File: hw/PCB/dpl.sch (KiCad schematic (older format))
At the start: 1 part

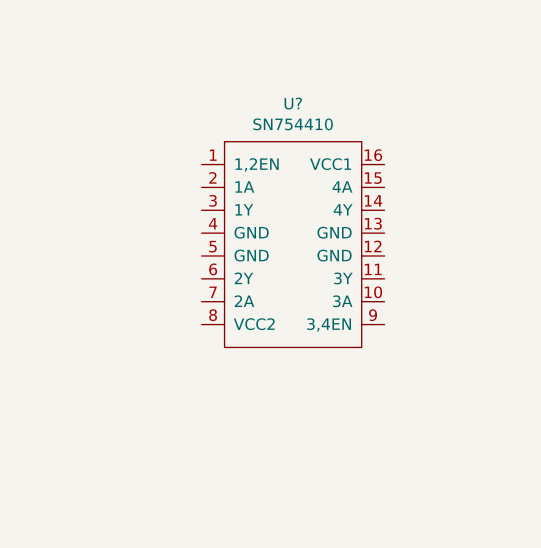
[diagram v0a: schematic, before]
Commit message: Added pin labels for the femto-satellite deploy system.
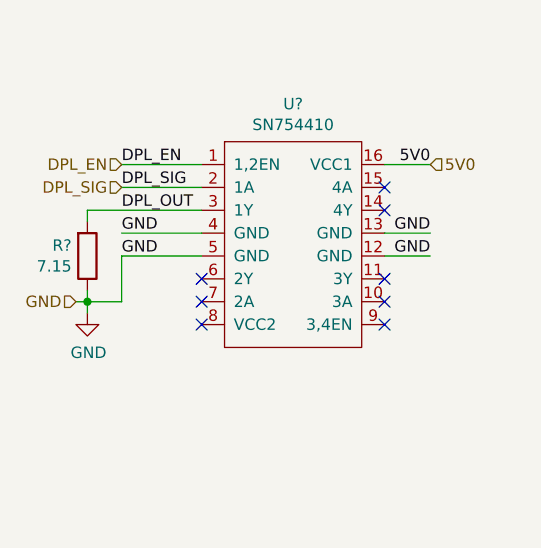
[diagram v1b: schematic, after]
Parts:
- added R?: 7.15, symbol Device:R
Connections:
- net DPL_EN: now reaches U?.1 (1,2EN)
- net GND: now reaches U?.12 (GND)
- net GND: now also U?.13 (GND), U?.4 (GND), U?.5 (GND), R?.1
- net 5V0: now reaches U?.16 (VCC1)
- net DPL_SIG: now reaches U?.2 (1A)
- net DPL_OUT: now reaches U?.3 (1Y)
- net DPL_OUT: now also R?.2
- no-connect marks 0 -> 8
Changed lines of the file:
@@
 	1    0    0    -1
 $EndComp
+$Comp
+L Device:R R?
+U 1 1 5BEA225C
+P 4750 3500
+F 0 "R?" H 4681 3454 50  0000 R CNN
+F 1 "7.15" H 4681 3545 50  0000 R CNN
+F 2 "" V 4680 3500 50  0001 C CNN
+F 3 "~" H 4750 3500 50  0001 C CNN
+	1    4750 3500
+	1    0    0    1
+$EndComp
+Wire Wire Line
+	6050 3100 6250 3100
+Text Label 6250 3100 2    50   ~ 0
+5V0
+Text Label 4900 3200 0    50   ~ 0
+DPL_SIG
+Text Label 4900 3100 0    50   ~ 0
+DPL_EN
+Text Label 4900 3300 0    50   ~ 0
+DPL_OUT
+Wire Wire Line
+	5250 3100 4900 3100
+Wire Wire Line
+	4900 3200 5250 3200
+Wire Wire Line
+	5250 3400 4900 3400
+Wire Wire Line
+	4900 3500 5250 3500
+Wire Wire Line
+	6050 3400 6250 3400
+Wire Wire Line
+	6250 3500 6050 3500
+Text Label 4900 3400 0    50   ~ 0
+GND
+Text Label 4900 3500 0    50   ~ 0
+GND
+Text Label 6250 3400 2    50   ~ 0
+GND
+Text Label 6250 3500 2    50   ~ 0
+GND
+Wire Wire Line
+	4750 3300 4750 3350
+Wire Wire Line
+	4750 3300 5250 3300
+Wire Wire Line
+	4750 3650 4750 3700
+Wire Wire Line
+	4750 3700 4900 3700
+Wire Wire Line
+	4900 3700 4900 3500
+Wire Wire Line
+	4750 3700 4750 3750
+Connection ~ 4750 3700
+$Comp
+L power:GND #PWR?
+U 1 1 5BEA3F1A
+P 4750 3750
+F 0 "#PWR?" H 4750 3500 50  0001 C CNN
+F 1 "GND" H 4755 3577 50  0000 C CNN
+F 2 "" H 4750 3750 50  0001 C CNN
+F 3 "" H 4750 3750 50  0001 C CNN
+	1    4750 3750
+	1    0    0    -1
+$EndComp
+Text HLabel 4900 3100 0    50   Input ~ 0
+DPL_EN
+Text HLabel 4900 3200 0    50   Input ~ 0
+DPL_SIG
+Text HLabel 4700 3700 0    50   Input ~ 0
+GND
+Wire Wire Line
+	4750 3700 4700 3700
+NoConn ~ 6050 3200
+NoConn ~ 6050 3300
+NoConn ~ 6050 3600
+NoConn ~ 6050 3700
+NoConn ~ 6050 3800
+NoConn ~ 5250 3600
+NoConn ~ 5250 3700
+NoConn ~ 5250 3800
+Text HLabel 6250 3100 2    50   Input ~ 0
+5V0
 $EndSCHEMATC

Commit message: Updated the connections and the footprints asignation.
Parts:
- U3: renamed from U?; footprint (none) -> Package_DIP:DIP-16_W7.62mm_Socket_LongPads
- gave numbers to parts that had none: 1
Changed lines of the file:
@@
 $EndDescr
 $Comp
-L H-Bridge:SN754410 U?
+L H-Bridge:SN754410 U3
 U 1 1 5BEA29D2
 P 5650 3450
-F 0 "U?" H 5650 4065 50  0000 C CNN
+F 0 "U3" H 5650 4065 50  0000 C CNN
 F 1 "SN754410" H 5650 3974 50  0000 C CNN
-F 2 "" H 5500 3550 50  0001 C CNN
+F 2 "Package_DIP:DIP-16_W7.62mm_Socket_LongPads" H 5500 3550 50  0001 C CNN
 F 3 "" H 5500 3550 50  0001 C CNN
 	1    5650 3450
@@
 $EndComp
 $Comp
-L Device:R R?
+L Device:R R3
 U 1 1 5BEA225C
 P 4750 3500
-F 0 "R?" H 4681 3454 50  0000 R CNN
+F 0 "R3" H 4681 3454 50  0000 R CNN
 F 1 "7.15" H 4681 3545 50  0000 R CNN
 F 2 "" V 4680 3500 50  0001 C CNN
@@
 Connection ~ 4750 3700
 $Comp
-L power:GND #PWR?
+L power:GND #PWR0112
 U 1 1 5BEA3F1A
 P 4750 3750
-F 0 "#PWR?" H 4750 3500 50  0001 C CNN
+F 0 "#PWR0112" H 4750 3500 50  0001 C CNN
 F 1 "GND" H 4755 3577 50  0000 C CNN
 F 2 "" H 4750 3750 50  0001 C CNN

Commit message: Added the deployment system to the board's footprint.
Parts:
- R3: footprint (none) -> Resistor_FOD:RCL12257R15FKEG
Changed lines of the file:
@@
 F 0 "R3" H 4681 3454 50  0000 R CNN
 F 1 "7.15" H 4681 3545 50  0000 R CNN
-F 2 "" V 4680 3500 50  0001 C CNN
+F 2 "Resistor_FOD:RCL12257R15FKEG" V 4680 3500 50  0001 C CNN
 F 3 "~" H 4750 3500 50  0001 C CNN
 	1    4750 3500

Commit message: Added new connections and 3D models. Most components are now placed in the PCB.
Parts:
- U3: footprint Package_DIP:DIP-16_W7.62mm_Socket_LongPads -> Package_DIP:DIP-16_W7.62mm_LongPads
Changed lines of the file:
@@
 F 0 "U3" H 5650 4065 50  0000 C CNN
 F 1 "SN754410" H 5650 3974 50  0000 C CNN
-F 2 "Package_DIP:DIP-16_W7.62mm_Socket_LongPads" H 5500 3550 50  0001 C CNN
+F 2 "Package_DIP:DIP-16_W7.62mm_LongPads" H 5500 3550 50  0001 C CNN
 F 3 "" H 5500 3550 50  0001 C CNN
 	1    5650 3450

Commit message: Added switch to detect the deplyment status. Routed all connections.
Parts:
- added R4: 1K, Resistor_SMD:R_0603_1608Metric_Pad1.05x0.95mm_HandSolder, symbol Device:R
- added U5: AV4524_2PIN, Interrupt:AV4524_2PIN, symbol Interrupter:AV4524_2PIN
- U3: footprint Package_DIP:DIP-16_W7.62mm_LongPads -> Package_DIP:DIP-16_W7.62mm
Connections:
- net GND: now also U5.1 (COM)
- net 5V0 renamed VCC
- net VCC: now also R4.2
- new net DPL_STA: R4.1, U5.2 (NO)
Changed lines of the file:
@@
 F 0 "U3" H 5650 4065 50  0000 C CNN
 F 1 "SN754410" H 5650 3974 50  0000 C CNN
-F 2 "Package_DIP:DIP-16_W7.62mm_LongPads" H 5500 3550 50  0001 C CNN
+F 2 "Package_DIP:DIP-16_W7.62mm" H 5500 3550 50  0001 C CNN
 F 3 "" H 5500 3550 50  0001 C CNN
 	1    5650 3450
@@
 	6050 3100 6250 3100
 Text Label 6250 3100 2    50   ~ 0
-5V0
+VCC
 Text Label 4900 3200 0    50   ~ 0
 DPL_SIG
@@
 NoConn ~ 5250 3800
 Text HLabel 6250 3100 2    50   Input ~ 0
-5V0
+VCC
+$Comp
+L Device:R R4
+U 1 1 5BF60B18
+P 5150 4300
+F 0 "R4" H 5081 4254 50  0000 R CNN
+F 1 "1K" H 5081 4345 50  0000 R CNN
+F 2 "Resistor_SMD:R_0603_1608Metric_Pad1.05x0.95mm_HandSolder" V 5080 4300 50  0001 C CNN
+F 3 "~" H 5150 4300 50  0001 C CNN
+	1    5150 4300
+	1    0    0    1
+$EndComp
+Text Label 5250 4500 0    50   ~ 0
+DPL_STA
+Wire Wire Line
+	5250 4400 5550 4400
+Text Label 5250 4400 0    50   ~ 0
+GND
+Text Label 5000 4150 0    50   ~ 0
+VCC
+Wire Wire Line
+	5150 4150 5000 4150
+Wire Wire Line
+	5150 4500 5150 4450
+Wire Wire Line
+	5150 4500 5550 4500
+Wire Wire Line
+	5150 4500 5100 4500
+Connection ~ 5150 4500
+Text HLabel 5100 4500 0    50   Input ~ 0
+DPL_STA
+$Comp
+L Interrupter:AV4524_2PIN U5
+U 1 1 5BF65EF1
+P 5750 4500
+F 0 "U5" H 6028 4546 50  0000 L CNN
+F 1 "AV4524_2PIN" H 6028 4455 50  0000 L CNN
+F 2 "Interrupt:AV4524_2PIN" H 5700 4500 50  0001 C CNN
+F 3 "" H 5700 4500 50  0001 C CNN
+	1    5750 4500
+	1    0    0    -1
+$EndComp
 $EndSCHEMATC

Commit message: Finished preliminary design phase for the version 2.0.
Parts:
- removed R3: 7.15, Resistor_FOD:RCL12257R15FKEG, symbol Device:R
- removed R4: 1K, Resistor_SMD:R_0603_1608Metric_Pad1.05x0.95mm_HandSolder, symbol Device:R
- removed U3: SN754410, Package_DIP:DIP-16_W7.62mm, symbol H-Bridge:SN754410
- removed U5: AV4524_2PIN, Interrupt:AV4524_2PIN, symbol Interrupter:AV4524_2PIN
- added D2: LED, Diode_SMD:D_0805_2012Metric_Pad1.15x1.40mm_HandSolder, symbol Device:LED
- added J3: Nichrome, TerminalBlock:TerminalBlock_Altech_AK300-2_P5.00mm, symbol Connector:Screw_Terminal_01x02
- added Q1: PMV16XNR, Package_TO_SOT_SMD:SOT-23, symbol Transistor_FET:2N7002
- added R5: 330, Resistor_SMD:R_0603_1608Metric_Pad1.05x0.95mm_HandSolder, symbol Device:R
- added U4: AV4524, Interrupt:AV4524, symbol Interrupter:AV4524
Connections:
- net DPL_EN: now also D2.2 (A)
- net DPL_STA: now also U4.1 (COM)
- net GND: now also Q1.2 (S), R5.2, U4.3 (NC)
- new net: J3.2 (Pin_2), Q1.3 (D)
- new net: D2.1 (K), Q1.1 (G), R5.1
- new net 3V3: U4.2 (NO)
- new net VIN: J3.1 (Pin_1)
- no-connect marks 8 -> 0
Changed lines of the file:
@@
 EESchema Schematic File Version 5
-LIBS:FOD-cache
 EELAYER 29 0
 EELAYER END
 $Descr A4 11693 8268
 encoding utf-8
-Sheet 5 5
+Sheet 5 6
 Title ""
 Date ""
@@
 $EndDescr
 $Comp
-L H-Bridge:SN754410 U3
-U 1 1 5BEA29D2
-P 5650 3450
-F 0 "U3" H 5650 4065 50  0000 C CNN
-F 1 "SN754410" H 5650 3974 50  0000 C CNN
-F 2 "Package_DIP:DIP-16_W7.62mm" H 5500 3550 50  0001 C CNN
-F 3 "" H 5500 3550 50  0001 C CNN
-	1    5650 3450
+L power:GND #PWR0112
+U 1 1 5BEA3F1A
+P 5750 3150
+F 0 "#PWR0112" H 5750 2900 50  0001 C CNN
+F 1 "GND" H 5755 2977 50  0000 C CNN
+F 2 "" H 5750 3150 50  0001 C CNN
+F 3 "" H 5750 3150 50  0001 C CNN
+	1    5750 3150
+	1    0    0    -1
+$EndComp
+Text HLabel 4950 2900 0    50   Input ~ 0
+DPL_EN
+Text HLabel 4950 3950 0    50   Input ~ 0
+GND
+Text HLabel 5750 2550 0    50   Input ~ 0
+VIN
+Text HLabel 4950 3750 0    50   Input ~ 0
+DPL_STA
+$Comp
+L Connector:Screw_Terminal_01x02 J3
+U 1 1 5D23C1A6
+P 6150 2550
+F 0 "J3" H 6230 2542 50  0000 L CNN
+F 1 "Nichrome" H 6230 2451 50  0000 L CNN
+F 2 "TerminalBlock:TerminalBlock_Altech_AK300-2_P5.00mm" H 6150 2550 50  0001 C CNN
+F 3 "~" H 6150 2550 50  0001 C CNN
+	1    6150 2550
+	1    0    0    -1
+$EndComp
+Wire Wire Line
+	5750 2650 5750 2700
+Wire Wire Line
+	5750 2650 5950 2650
+Wire Wire Line
+	5950 2550 5750 2550
+Wire Wire Line
+	5750 3150 5750 3100
+$Comp
+L Interrupter:AV4524 U4
+U 1 1 5D23F1CD
+P 5350 3850
+F 0 "U4" H 5628 3896 50  0000 L CNN
+F 1 "AV4524" H 5628 3805 50  0000 L CNN
+F 2 "Interrupt:AV4524" H 5300 3850 50  0001 C CNN
+F 3 "" H 5300 3850 50  0001 C CNN
+	1    5350 3850
+	1    0    0    -1
+$EndComp
+Wire Wire Line
+	5150 3750 4950 3750
+Wire Wire Line
+	5150 3950 5050 3950
+Wire Wire Line
+	4950 3850 5150 3850
+Text HLabel 4950 3850 0    50   Input ~ 0
+3V3
+$Comp
+L power:GND #PWR0117
+U 1 1 5D2408D3
+P 5050 4000
+F 0 "#PWR0117" H 5050 3750 50  0001 C CNN
+F 1 "GND" H 5055 3827 50  0000 C CNN
+F 2 "" H 5050 4000 50  0001 C CNN
+F 3 "" H 5050 4000 50  0001 C CNN
+	1    5050 4000
+	1    0    0    -1
+$EndComp
+Wire Wire Line
+	5050 4000 5050 3950
+Connection ~ 5050 3950
+Wire Wire Line
+	5050 3950 4950 3950
+$Comp
+L Device:R R5
+U 1 1 5D23EA26
+P 5350 3100
+F 0 "R5" H 5420 3146 50  0000 L CNN
+F 1 "330" H 5420 3055 50  0000 L CNN
+F 2 "Resistor_SMD:R_0603_1608Metric_Pad1.05x0.95mm_HandSolder" V 5280 3100 50  0001 C CNN
+F 3 "~" H 5350 3100 50  0001 C CNN
+	1    5350 3100
 	1    0    0    -1
 $EndComp
 $Comp
-L Device:R R3
-U 1 1 5BEA225C
-P 4750 3500
-F 0 "R3" H 4681 3454 50  0000 R CNN
-F 1 "7.15" H 4681 3545 50  0000 R CNN
-F 2 "Resistor_FOD:RCL12257R15FKEG" V 4680 3500 50  0001 C CNN
-F 3 "~" H 4750 3500 50  0001 C CNN
-	1    4750 3500
-	1    0    0    1
+L Device:LED D2
+U 1 1 5D23EB22
+P 5150 2900
+F 0 "D2" H 5143 2645 50  0000 C CNN
+F 1 "LED" H 5143 2736 50  0000 C CNN
+F 2 "Diode_SMD:D_0805_2012Metric_Pad1.15x1.40mm_HandSolder" H 5150 2900 50  0001 C CNN
+F 3 "~" H 5150 2900 50  0001 C CNN
+	1    5150 2900
+	-1   0    0    1
 $EndComp
 Wire Wire Line
-	6050 3100 6250 3100
-Text Label 6250 3100 2    50   ~ 0
-VCC
-Text Label 4900 3200 0    50   ~ 0
-DPL_SIG
-Text Label 4900 3100 0    50   ~ 0
-DPL_EN
-Text Label 4900 3300 0    50   ~ 0
-DPL_OUT
+	5300 2900 5350 2900
 Wire Wire Line
-	5250 3100 4900 3100
+	5350 2900 5350 2950
 Wire Wire Line
-	4900 3200 5250 3200
-Wire Wire Line
-	5250 3400 4900 3400
-Wire Wire Line
-	4900 3500 5250 3500
-Wire Wire Line
-	6050 3400 6250 3400
-Wire Wire Line
-	6250 3500 6050 3500
-Text Label 4900 3400 0    50   ~ 0
-GND
-Text Label 4900 3500 0    50   ~ 0
-GND
-Text Label 6250 3400 2    50   ~ 0
-GND
-Text Label 6250 3500 2    50   ~ 0
-GND
-Wire Wire Line
-	4750 3300 4750 3350
-Wire Wire Line
-	4750 3300 5250 3300
-Wire Wire Line
-	4750 3650 4750 3700
-Wire Wire Line
-	4750 3700 4900 3700
-Wire Wire Line
-	4900 3700 4900 3500
-Wire Wire Line
-	4750 3700 4750 3750
-Connection ~ 4750 3700
+	5350 3250 5350 3300
 $Comp
-L power:GND #PWR0112
-U 1 1 5BEA3F1A
-P 4750 3750
-F 0 "#PWR0112" H 4750 3500 50  0001 C CNN
-F 1 "GND" H 4755 3577 50  0000 C CNN
-F 2 "" H 4750 3750 50  0001 C CNN
-F 3 "" H 4750 3750 50  0001 C CNN
-	1    4750 3750
+L power:GND #PWR0118
+U 1 1 5D23F136
+P 5350 3300
+F 0 "#PWR0118" H 5350 3050 50  0001 C CNN
+F 1 "GND" H 5355 3127 50  0000 C CNN
+F 2 "" H 5350 3300 50  0001 C CNN
+F 3 "" H 5350 3300 50  0001 C CNN
+	1    5350 3300
 	1    0    0    -1
 $EndComp
-Text HLabel 4900 3100 0    50   Input ~ 0
-DPL_EN
-Text HLabel 4900 3200 0    50   Input ~ 0
-DPL_SIG
-Text HLabel 4700 3700 0    50   Input ~ 0
-GND
 Wire Wire Line
-	4750 3700 4700 3700
-NoConn ~ 6050 3200
-NoConn ~ 6050 3300
-NoConn ~ 6050 3600
-NoConn ~ 6050 3700
-NoConn ~ 6050 3800
-NoConn ~ 5250 3600
-NoConn ~ 5250 3700
-NoConn ~ 5250 3800
-Text HLabel 6250 3100 2    50   Input ~ 0
-VCC
+	4950 2900 5000 2900
+Wire Wire Line
+	5350 2900 5450 2900
+Connection ~ 5350 2900
 $Comp
-L Device:R R4
-U 1 1 5BF60B18
-P 5150 4300
-F 0 "R4" H 5081 4254 50  0000 R CNN
-F 1 "1K" H 5081 4345 50  0000 R CNN
-F 2 "Resistor_SMD:R_0603_1608Metric_Pad1.05x0.95mm_HandSolder" V 5080 4300 50  0001 C CNN
-F 3 "~" H 5150 4300 50  0001 C CNN
-	1    5150 4300
-	1    0    0    1
-$EndComp
-Text Label 5250 4500 0    50   ~ 0
-DPL_STA
-Wire Wire Line
-	5250 4400 5550 4400
-Text Label 5250 4400 0    50   ~ 0
-GND
-Text Label 5000 4150 0    50   ~ 0
-VCC
-Wire Wire Line
-	5150 4150 5000 4150
-Wire Wire Line
-	5150 4500 5150 4450
-Wire Wire Line
-	5150 4500 5550 4500
-Wire Wire Line
-	5150 4500 5100 4500
-Connection ~ 5150 4500
-Text HLabel 5100 4500 0    50   Input ~ 0
-DPL_STA
-$Comp
-L Interrupter:AV4524_2PIN U5
-U 1 1 5BF65EF1
-P 5750 4500
-F 0 "U5" H 6028 4546 50  0000 L CNN
-F 1 "AV4524_2PIN" H 6028 4455 50  0000 L CNN
-F 2 "Interrupt:AV4524_2PIN" H 5700 4500 50  0001 C CNN
-F 3 "" H 5700 4500 50  0001 C CNN
-	1    5750 4500
+L Transistor_FET:2N7002 Q1
+U 1 1 5D257A79
+P 5650 2900
+F 0 "Q1" H 5856 2946 50  0000 L CNN
+F 1 "PMV16XNR" H 5856 2855 50  0000 L CNN
+F 2 "Package_TO_SOT_SMD:SOT-23" H 5850 2825 50  0001 L CIN
+F 3 "https://www.fairchildsemi.com/datasheets/2N/2N7002.pdf" H 5650 2900 50  0001 L CNN
+	1    5650 2900
 	1    0    0    -1
 $EndComp
